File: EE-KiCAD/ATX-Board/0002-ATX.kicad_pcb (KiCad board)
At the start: 2 copper layers, 117 x 77 mm, 91 parts, among them J101 Screw_Terminal_01x01, J102 Screw_Terminal_01x01, J103 Screw_Terminal_01x01, J104 Screw_Terminal_01x01, J105 Conn_01x03, J106 Conn_01x04, J107 Conn_02x04_Top_Bottom, J108 Conn_02x04_Top_Bottom, J109 Conn_02x04_Top_Bottom, J110 Conn_02x04_Top_Bottom, J111 Conn_02x04_Top_Bottom, J112 Conn_02x04_Top_Bottom, J113 Conn_02x04_Top_Bottom, J114 Conn_02x03_Top_Bottom, J115 Conn_02x03_Top_Bottom, J116 Conn_02x03_Top_Bottom, J117 Conn_02x03_Top_Bottom, J118 Conn_02x05_Top_Bottom, J119 Conn_02x09_Top_Bottom, Q1 BSC026N08NS5ATMA1, Q101 BSC026N08NS5ATMA1, Q102 BSC026N08NS5ATMA1, Q103 BSC026N08NS5ATMA1, Q104 BSC026N08NS5ATMA1, Q109 2N7002E, Q2 BSC026N08NS5ATMA1, Q3 BSC026N08NS5ATMA1, Q4 BSC026N08NS5ATMA1, U1 TPS53015, U101 TPS56220X, U102 TPS53015, U104 7402

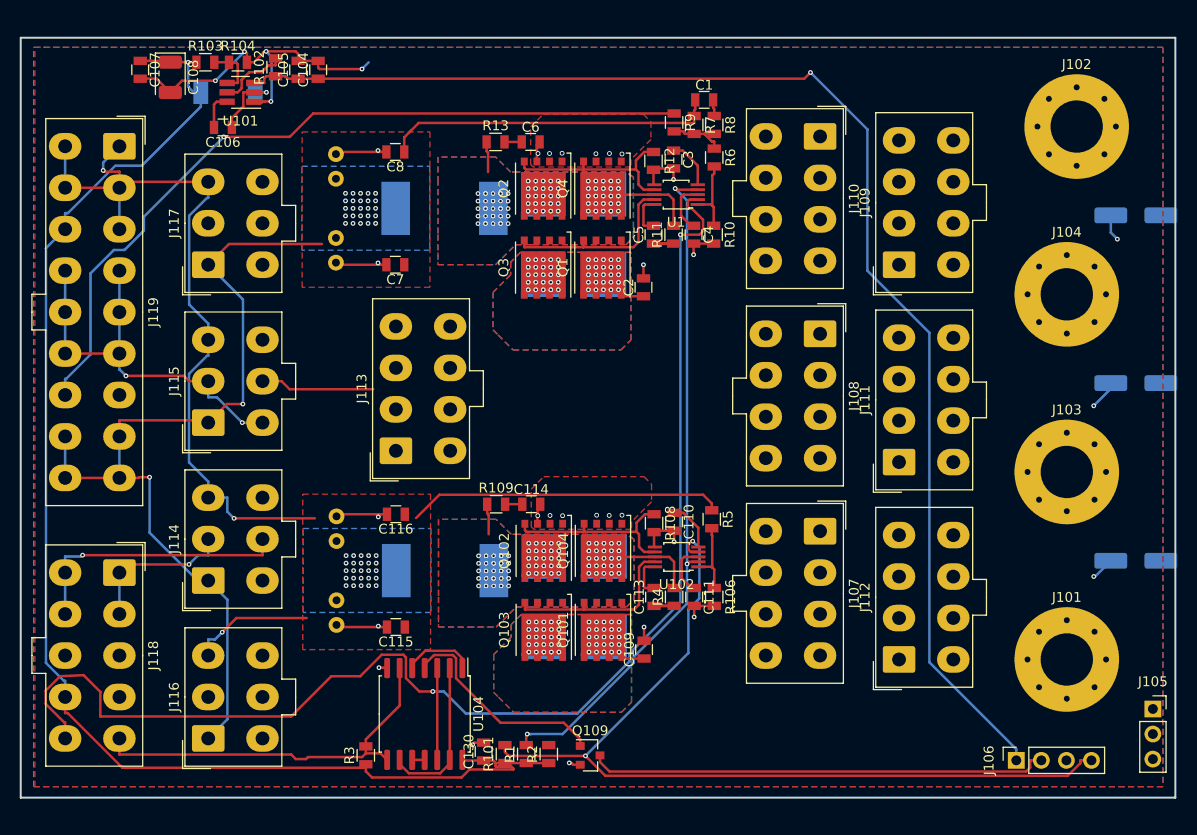
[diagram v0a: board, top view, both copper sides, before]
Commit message: Finish first draft of PCBs.  Pulled PCBs into OpenSCAD for fitment.
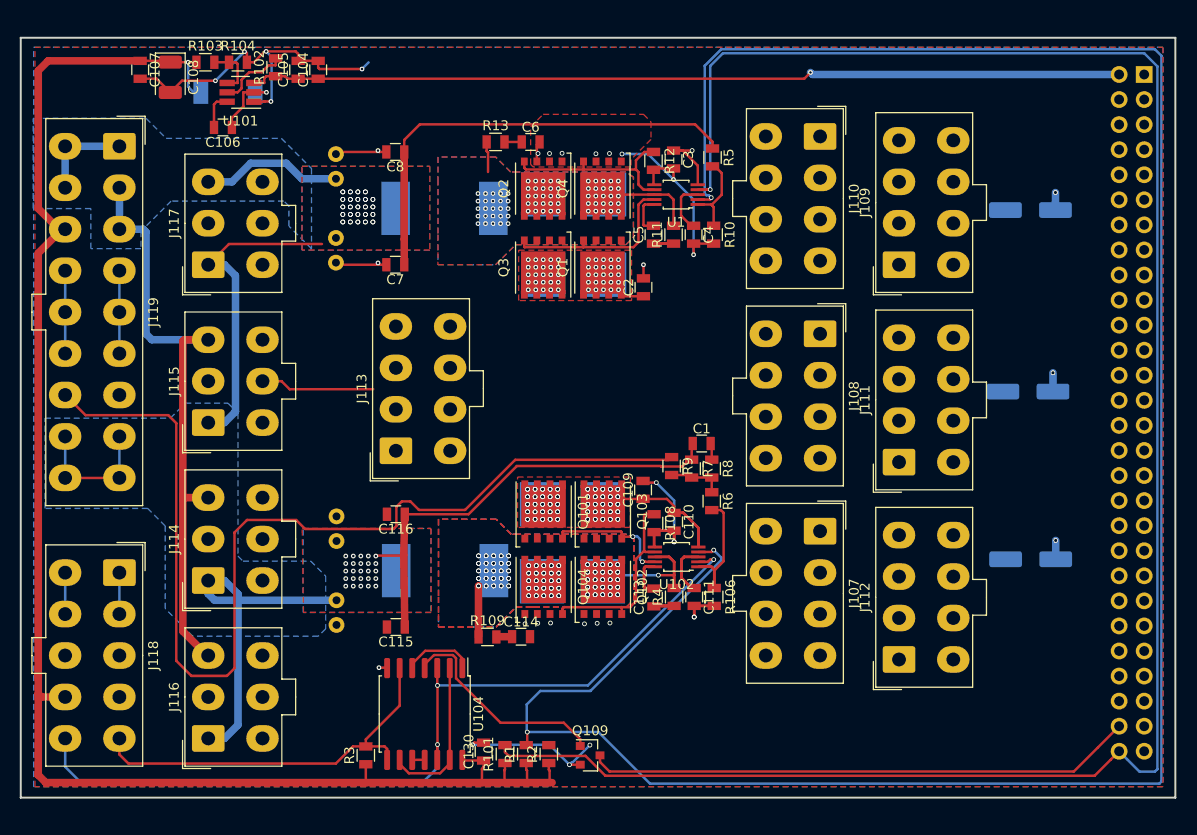
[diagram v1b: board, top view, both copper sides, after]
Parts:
- removed J101, J102, J103, J104: Screw_Terminal_01x01, Mounting_Holes:MountingHole_5.3mm_M5_Pad_Via
- removed J105: Conn_01x03, Connector_PinSocket_2.54mm:PinSocket_1x03_P2.54mm_Vertical
- removed J106: Conn_01x04, Connector_PinSocket_2.54mm:PinSocket_1x04_P2.54mm_Vertical
- added J200: Conn_02x28_Odd_Even, Connector_PinHeader_2.54mm:PinHeader_2x28_P2.54mm_Vertical, B.Cu at (203.8, 63.7)
- J107, J108, J109, J110, J111, J112, J113: footprint Connector_Molex:Molex_Mini-Fit_Jr_5566-08A_2x04_P4.20mm_Vertical -> ATXs:Molex_Mini-Fit_Jr_5566-08A_2x04_P4.20mm_Vertical
- J114, J115, J116, J117: footprint Connector_Molex:Molex_Mini-Fit_Jr_5566-06A_2x03_P4.20mm_Vertical -> ATXs:Molex_Mini-Fit_Jr_5566-06A_2x03_P4.20mm_Vertical
- J118: footprint Connector_Molex:Molex_Mini-Fit_Jr_5566-10A_2x05_P4.20mm_Vertical -> ATXs:Molex_Mini-Fit_Jr_5566-10A_2x05_P4.20mm_Vertical
- J119: footprint Connector_Molex:Molex_Mini-Fit_Jr_5566-18A_2x09_P4.20mm_Vertical -> ATXs:Molex_Mini-Fit_Jr_5566-18A_2x09_P4.20mm_Vertical
- moved R5 36.7 mm to (160.1, 72.1)
- moved C1 34.8 mm to (159.0, 101.1)
- moved R6 34.8 mm to (160.0, 107.0)
- moved R9 34.8 mm to (156.0, 103.4)
- moved R7 34.8 mm to (158.0, 103.7)
- moved R8 34.8 mm to (160.0, 103.7)
- moved C109 16.2 mm to (153.1, 105.8)
- moved HS103 14.9 mm to (142.8, 107.3), turned to 180 degrees
- moved HS104 14.7 mm to (149.0, 107.3), turned to 180 degrees
- moved R109 13.5 mm to (137.3, 120.7)
- moved C114 13.5 mm to (140.7, 120.7)
- moved Q101 13.4 mm to (143.0, 108.0), turned to 90 degrees
- moved Q103 13.4 mm to (149.0, 108.0), turned to 90 degrees
- moved C101 11.0 mm to (192.1, 95.9)
- moved C103 10.7 mm to (192.3, 77.5)
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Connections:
- C10 pad 1: 3V3 -> 5V
- C115 pad 1: 5V -> 3V3
- C116 pad 1: 5V -> 3V3
- C117 pad 1: 5V -> 3V3
- C118 pad 1: 5V -> 3V3
- C7 pad 1: 3V3 -> 5V
- C8 pad 1: 3V3 -> 5V
- C9 pad 1: 3V3 -> 5V
- L1 pad 2: 3V3 -> 5V
- L102 pad 2: 5V -> 3V3
- R1 pad 2: /sheet603813B5/EN -> /5V/EN
- R5 pad 2: /5V/FB -> /sheet603813B5/FB
- R6 pad 2: /sheet603813B5/FB -> /5V/FB
- U1 pad 2: /24pinATX/PWOK -> /5V/EN
- U1 pad 4: /sheet603813B5/EN -> PWOK
- U102 pad 2: /sheet603813B5/EN -> /24pinATX/PWOK
- U102 pad 4: PWOK -> /5V/EN
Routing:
- net /5V/EN: track 0.00 -> 235.5 mm, vias 0 -> 3
- net PWOK: track 91.0 -> 201.2 mm, vias 2 -> 1
- net /sheet603813B5/EN: track 69.4 -> 0.00 mm, vias 3 -> 0
- net /24pinATX/PWOK: track 139.6 -> 88.5 mm, vias 2 -> 3
- net Vstby: track 135.7 -> 88.7 mm
- net 3V3-RS: track 80.1 -> 107.2 mm, vias 1 -> 0
- net 5Vsb: track 142.4 -> 164.1 mm
- net Vmain: track 61.8 -> 48.2 mm, vias 104 -> 151
- net 5V: track 121.7 -> 132.1 mm, vias 28 -> 48
- net Net-(HS101-Pad1): track 13.2 -> 22.6 mm, vias 75 -> 151
- net PSON: track 46.7 -> 55.6 mm
- net /5V/FB: track 7.61 -> 14.7 mm
- net Net-(Q101-Pad4): track 18.8 -> 13.1 mm, vias 0 -> 2
- net Net-(C111-Pad1): track 5.38 -> 10.8 mm
- net Net-(C113-Pad2): track 4.15 -> 8.30 mm
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- removed copper zone on B.Cu, net GND

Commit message: add tabs on PCBs to set where they are in the box.  Box adjustments.
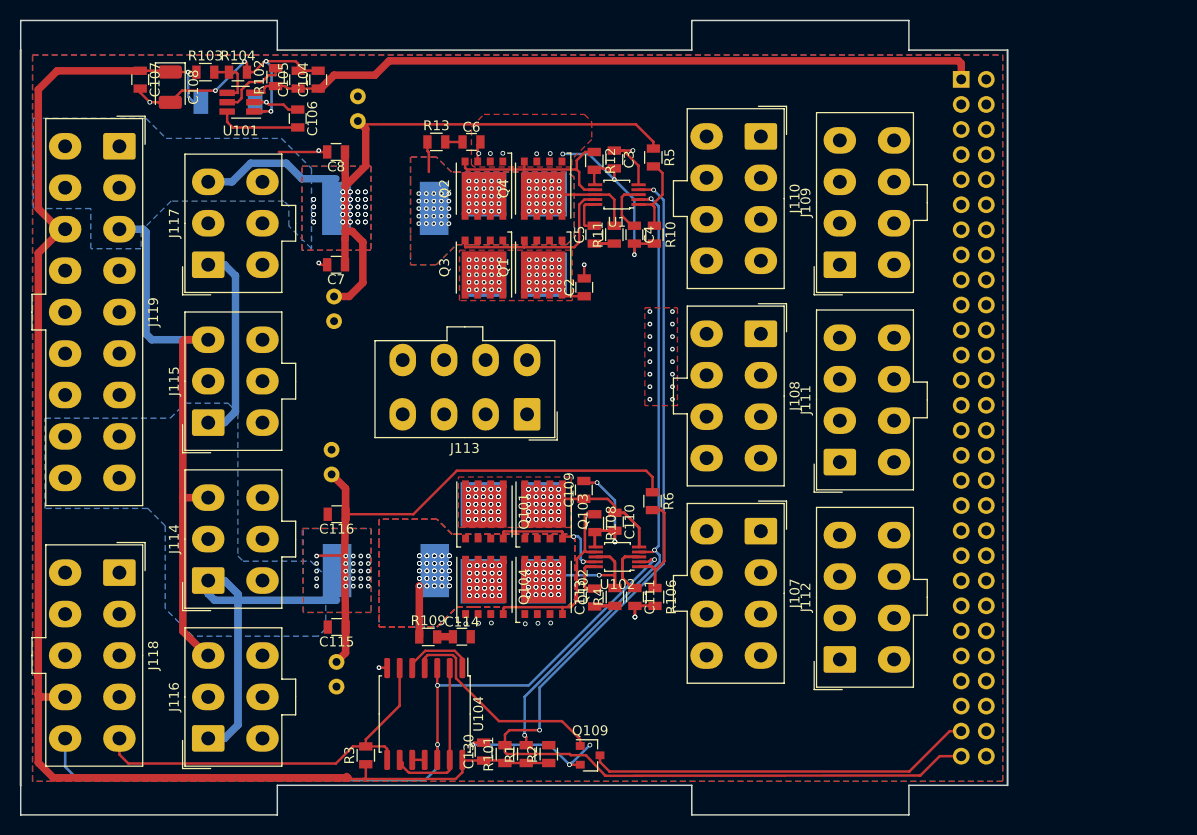
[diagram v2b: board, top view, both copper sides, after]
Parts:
- removed C1: 10uF, AEvan:0805_C
- removed C101, C102, C103: C, Capacitor_SMD:C_Elec_6.3x5.4
- removed R7: 10K, AEvan:0805_R
- removed R8: 10, AEvan:0805_R
- removed R9: 1k, AEvan:0805_R
- J200: footprint Connector_PinHeader_2.54mm:PinHeader_2x28_P2.54mm_Vertical -> Connector_PinSocket_2.54mm:PinSocket_2x28_P2.54mm_Horizontal
- moved J200 18.5 mm to (185.3, 64.2)
- moved J113 13.8 mm to (141.3, 98.2), turned to 180 degrees
- moved C106 7.63 mm to (118.1, 68.2), turned to 270 degrees
- moved C118 6.77 mm to (121.5, 104.2)
- moved C10 6.26 mm to (124.2, 68.4)
- moved C117 6.25 mm to (122.0, 123.2)
- moved C109 6.00 mm to (147.1, 105.8)
- moved C110 6.00 mm to (150.2, 109.0)
- moved C111 6.00 mm to (152.2, 116.7)
- moved C113 6.00 mm to (148.2, 116.7)
- moved C114 6.00 mm to (134.7, 120.7)
- moved C2 6.00 mm to (147.1, 85.3)
- moved C3 6.00 mm to (150.2, 72.3)
- moved C4 6.00 mm to (152.2, 80.0)
- moved C5 6.00 mm to (148.1, 80.0)
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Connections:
- J200 pad 1: Vmain -> Vstby
- J200 pad 2: Vstby -> Vmain
- J200 pad 53: SDA -> PSON
- J200 pad 54: PSON -> SDA
- J200 pad 55: SCL -> PWOK
- J200 pad 56: PWOK -> SCL
- R6 pad 1: Net-(R6-Pad1) -> 3V3
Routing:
- net /5V/EN: track 235.5 -> 64.8 mm
- net 3V3-RS: track 107.2 -> 0.00 mm
- net PWOK: track 201.2 -> 115.4 mm, vias 1 -> 2
- net GND: track 141.4 -> 102.9 mm, vias 34 -> 31
- net PSON: track 55.6 -> 39.4 mm
- net 3V3: track 128.9 -> 112.8 mm
- net Vmain: track 48.2 -> 32.4 mm, vias 151 -> 167
- net Vstby: track 88.7 -> 75.2 mm, vias 1 -> 0
- net 5Vsb: track 164.1 -> 153.9 mm
- net /24pinATX/PWOK: track 88.5 -> 82.3 mm
- net Net-(R6-Pad1): track 5.66 -> 0.00 mm
- net Net-(C106-Pad2): track 3.78 -> 8.43 mm
- net Net-(C1-Pad2): track 1.68 -> 0.00 mm
- net Net-(C106-Pad1): track 7.54 -> 5.92 mm
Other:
- board size 117 x 77 mm -> 100 x 80.5 mm
